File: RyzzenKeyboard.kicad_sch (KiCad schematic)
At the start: 0 parts

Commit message: [ADD](bank) added first 8 key bank
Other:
- added sheet key_bank (key_bank.kicad_sch)
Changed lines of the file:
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@@
 	(generator_version "9.0")
 	(paper "A4")
+	(sheet
+		(at 101.6 80.01)
+		(size 41.91 27.94)
+		(exclude_from_sim no)
+		(in_bom yes)
+		(on_board yes)
+		(dnp no)
+		(fields_autoplaced yes)
+		(stroke
+			(width 0.1524)
+			(type solid)
+		)
+		(fill
+			(color 0 0 0 0.0000)
+		)
+		(property "Sheetname" "key_bank"
+			(at 101.6 79.2984 0)
+			(effects
+				(font
+					(size 1.27 1.27)
+				)
+				(justify left bottom)
+			)
+		)
+		(property "Sheetfile" "key_bank.kicad_sch"
+			(at 101.6 108.5346 0)
+			(effects
+				(font
+					(size 1.27 1.27)
+				)
+				(justify left top)
+			)
+		)
+		(instances
+			(project "RyzzenKeyboard"
+				(path "/5d44d704-6136-40a8-98a4-93f001ea8743"
+					(page "2")
+				)
+			)
+		)
+	)
 	(sheet_instances
 		(path "/"

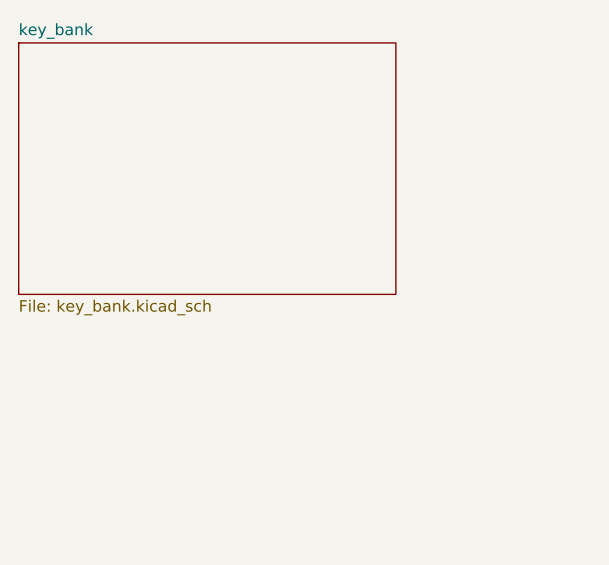
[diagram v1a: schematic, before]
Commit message: [ADD](keys) added keys subsheet
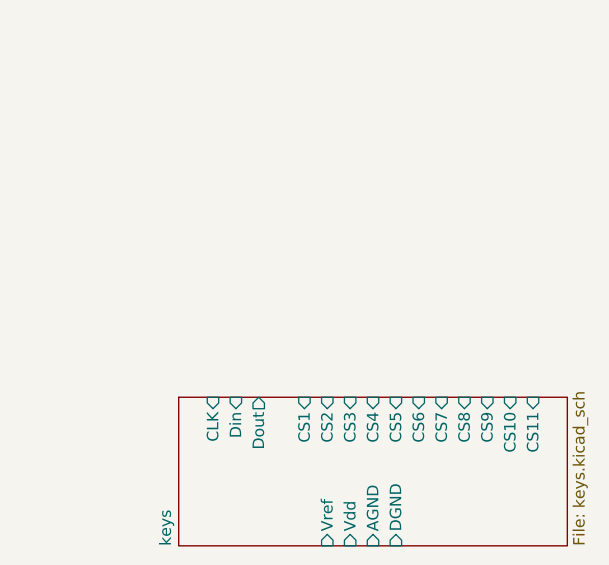
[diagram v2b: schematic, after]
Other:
- removed sheet key_bank
- added sheet keys (keys.kicad_sch)
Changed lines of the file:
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@@
 	(paper "A4")
 	(sheet
-		(at 101.6 80.01)
-		(size 41.91 27.94)
+		(at 119.38 119.38)
+		(size 43.18 16.51)
 		(exclude_from_sim no)
 		(in_bom yes)
@@
 			(color 0 0 0 0.0000)
 		)
-		(property "Sheetname" "key_bank"
-			(at 101.6 79.2984 0)
+		(property "Sheetname" "keys"
+			(at 118.6684 135.89 90)
 			(effects
 				(font
@@
 			)
 		)
-		(property "Sheetfile" "key_bank.kicad_sch"
-			(at 101.6 108.5346 0)
+		(property "Sheetfile" "keys.kicad_sch"
+			(at 163.1446 135.89 90)
 			(effects
 				(font
@@
 				)
 				(justify left top)
+			)
+		)
+		(pin "CLK" input
+			(at 123.19 119.38 90)
+			(effects
+				(font
+					(size 1.27 1.27)
+				)
+				(justify right)
+			)
+		)
+		(pin "Din" input
+			(at 125.73 119.38 90)
+			(effects
+				(font
+					(size 1.27 1.27)
+				)
+				(justify right)
+			)
+		)
+		(pin "Dout" output
+			(at 128.27 119.38 90)
+			(effects
+				(font
+					(size 1.27 1.27)
+				)
+				(justify right)
+			)
+		)
+		(pin "CS1" input
+			(at 133.35 119.38 90)
+			(effects
+				(font
+					(size 1.27 1.27)
+				)
+				(justify right)
+			)
+		)
+		(pin "CS2" input
+			(at 135.89 119.38 90)
+			(effects
+				(font
+					(size 1.27 1.27)
+				)
+				(justify right)
+			)
+		)
+		(pin "CS3" input
+			(at 138.43 119.38 90)
+			(effects
+				(font
+					(size 1.27 1.27)
+				)
+				(justify right)
+			)
+		)
+		(pin "CS4" input
+			(at 140.97 119.38 90)
+			(effects
+				(font
+					(size 1.27 1.27)
+				)
+				(justify right)
+			)
+		)
+		(pin "CS5" input
+			(at 143.51 119.38 90)
+			(effects
+				(font
+					(size 1.27 1.27)
+				)
+				(justify right)
+			)
+		)
+		(pin "CS6" input
+			(at 146.05 119.38 90)
+			(effects
+				(font
+					(size 1.27 1.27)
+				)
+				(justify right)
+			)
+		)
+		(pin "CS7" input
+			(at 148.59 119.38 90)
+			(effects
+				(font
+					(size 1.27 1.27)
+				)
+				(justify right)
+			)
+		)
+		(pin "CS8" input
+			(at 151.13 119.38 90)
+			(effects
+				(font
+					(size 1.27 1.27)
+				)
+				(justify right)
+			)
+		)
+		(pin "CS9" input
+			(at 153.67 119.38 90)
+			(effects
+				(font
+					(size 1.27 1.27)
+				)
+				(justify right)
+			)
+		)
+		(pin "CS10" input
+			(at 156.21 119.38 90)
+			(effects
+				(font
+					(size 1.27 1.27)
+				)
+				(justify right)
+			)
+		)
+		(pin "CS11" input
+			(at 158.75 119.38 90)
+			(effects
+				(font
+					(size 1.27 1.27)
+				)
+				(justify right)
+			)
+		)
+		(pin "Vref" input
+			(at 135.89 135.89 270)
+			(effects
+				(font
+					(size 1.27 1.27)
+				)
+				(justify left)
+			)
+		)
+		(pin "Vdd" input
+			(at 138.43 135.89 270)
+			(effects
+				(font
+					(size 1.27 1.27)
+				)
+				(justify left)
+			)
+		)
+		(pin "AGND" input
+			(at 140.97 135.89 270)
+			(effects
+				(font
+					(size 1.27 1.27)
+				)
+				(justify left)
+			)
+		)
+		(pin "DGND" input
+			(at 143.51 135.89 270)
+			(effects
+				(font
+					(size 1.27 1.27)
+				)
+				(justify left)
 			)
 		)
@@
 			(project "RyzzenKeyboard"
 				(path "/5d44d704-6136-40a8-98a4-93f001ea8743"
-					(page "2")
-				)
-			)
+					(page "101")
+				)
+			)

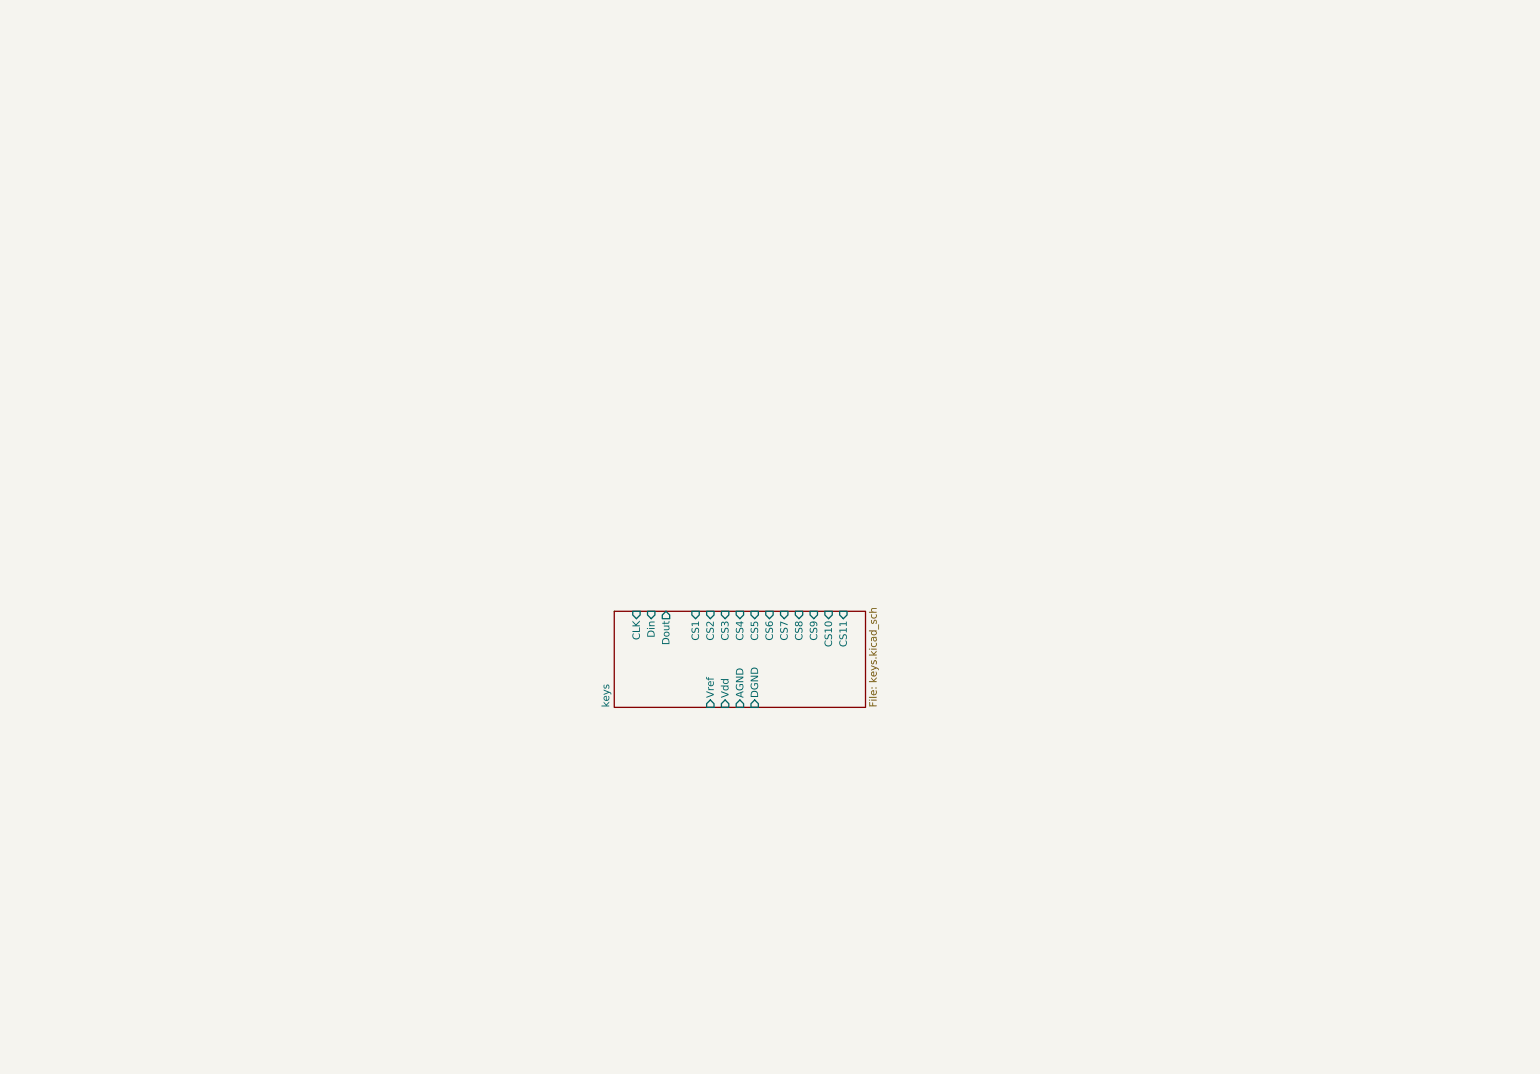
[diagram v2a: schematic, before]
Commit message: [ADD](mcu) added decoupling caps, boot reset and crystal
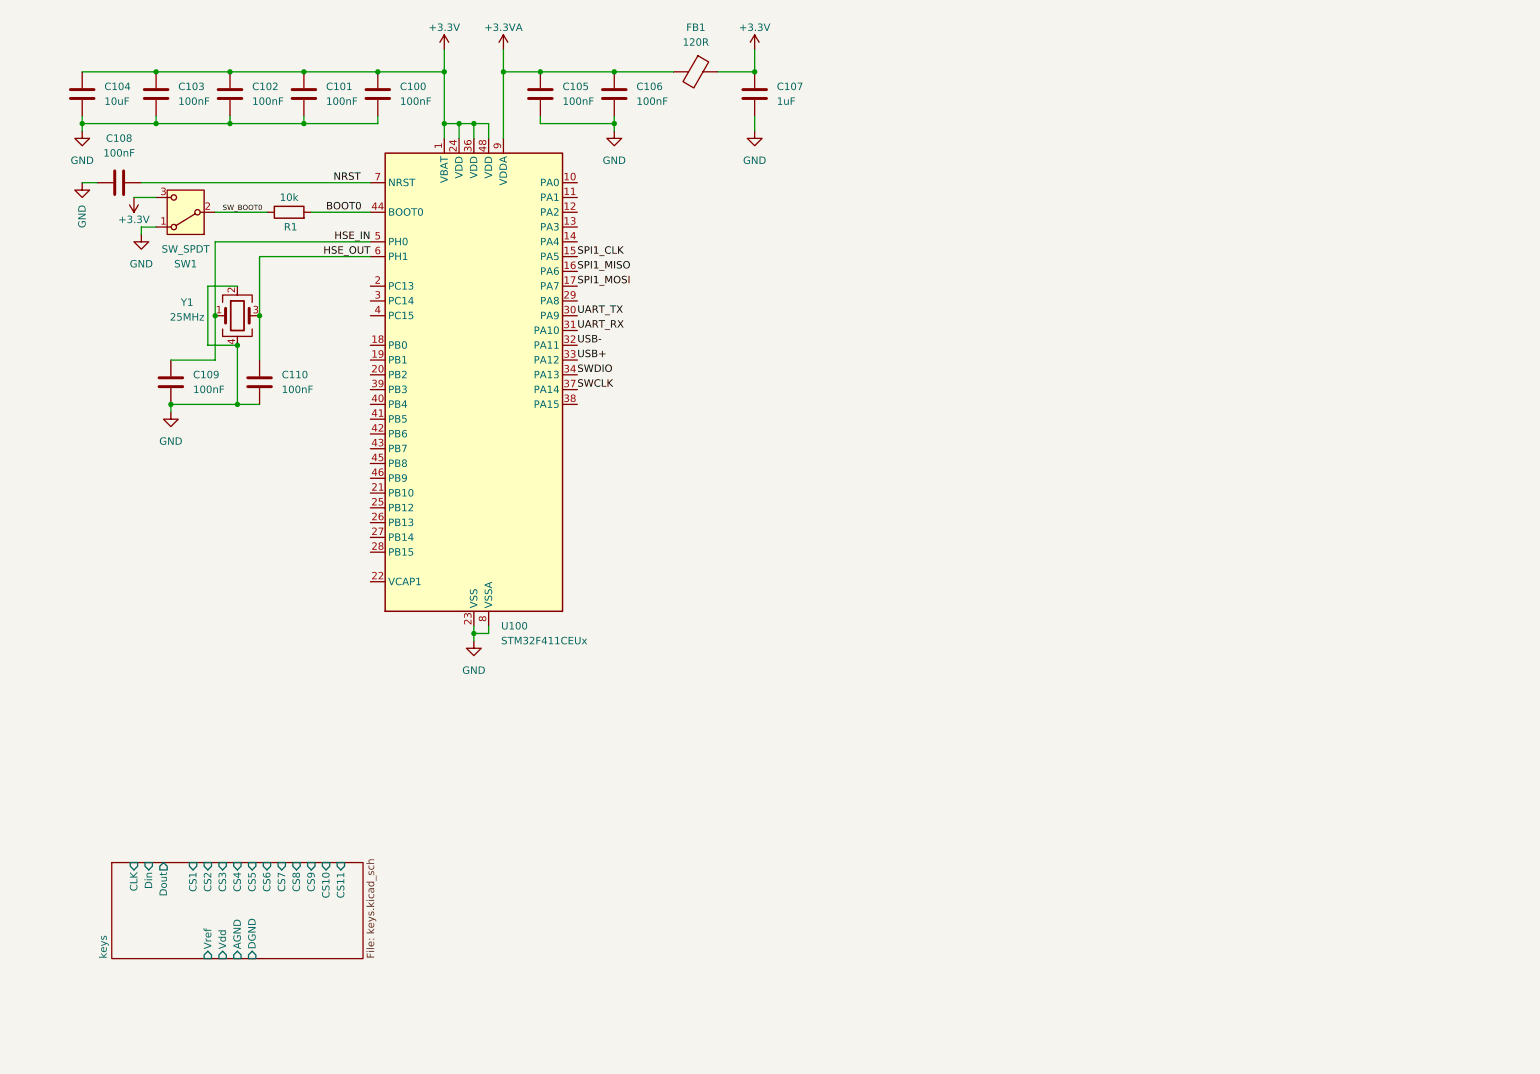
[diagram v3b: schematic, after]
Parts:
- added C100, C101, C102, C103, C105, C106, C108, C109, C110: 100nF, symbol Device:C
- added C104: 10uF, symbol Device:C
- added C107: 1uF, symbol Device:C
- added FB1: 120R, symbol Device:FerriteBead
- added R1: 10k, symbol Device:R
- added SW1: SW_SPDT, symbol Switch:SW_SPDT
- added U100: STM32F411CEUx, Package_DFN_QFN:QFN-48-1EP_7x7mm_P0.5mm_EP5.6x5.6mm, symbol MCU_ST_STM32F4:STM32F411CEUx
- added Y1: 25MHz, symbol Device:Crystal_GND24
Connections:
- new net +3.3V: C100.1, C101.1, C102.1, C103.1, C104.1, C107.1, FB1.1, SW1.3 (C), U100.1 (VBAT), U100.24 (VDD), U100.36 (VDD), U100.48 (VDD)
- new net +3.3VA: C105.1, C106.1, FB1.2, U100.9 (VDDA)
- new net BOOT0: R1.2, U100.44 (BOOT0)
- new net GND: C100.2, C101.2, C102.2, C103.2, C104.2, C105.2, C106.2, C107.2, C108.2, C109.2, C110.2, SW1.1 (A), U100.23 (VSS), U100.35 (VSS), U100.47 (VSS), U100.49 (VSS), U100.8 (VSSA), Y1.2, Y1.4
- new net HSE_IN: C109.1, U100.5 (PH0), Y1.1
- new net HSE_OUT: C110.1, U100.6 (PH1), Y1.3
- new net NRST: C108.1, U100.7 (NRST)
- new net SPI1_CLK: U100.15 (PA5)
- new net SPI1_MISO: U100.16 (PA6)
- new net SPI1_MOSI: U100.17 (PA7)
- new net SWCLK: U100.37 (PA14)
- new net SWDIO: U100.34 (PA13)
- new net SW_BOOT0: R1.1, SW1.2 (B)
- new net UART_RX: U100.31 (PA10)
- new net UART_TX: U100.30 (PA9)
- new net USB+: U100.33 (PA12)
- new net USB-: U100.32 (PA11)

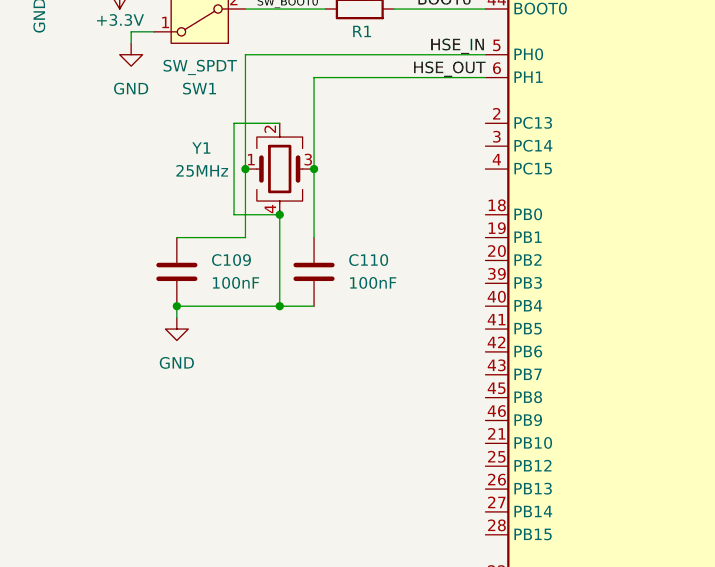
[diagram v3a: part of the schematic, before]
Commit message: [ADD](crystal) added values for the crystal's capacitors
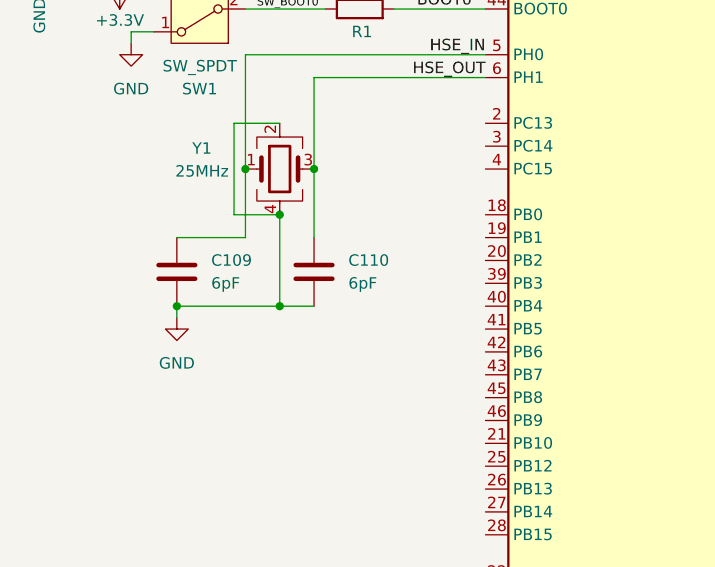
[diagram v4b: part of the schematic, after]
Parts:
- C109, C110: value 100nF -> 6pF
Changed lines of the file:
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@@
 			)
 		)
-		(property "Value" "100nF"
+		(property "Value" "6pF"
 			(at 46.99 81.2799 0)
 			(effects
@@
 			)
 		)
-		(property "Value" "100nF"
+		(property "Value" "6pF"
 			(at 62.23 81.2799 0)
 			(effects
